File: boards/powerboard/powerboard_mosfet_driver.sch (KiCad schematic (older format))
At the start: 3 parts

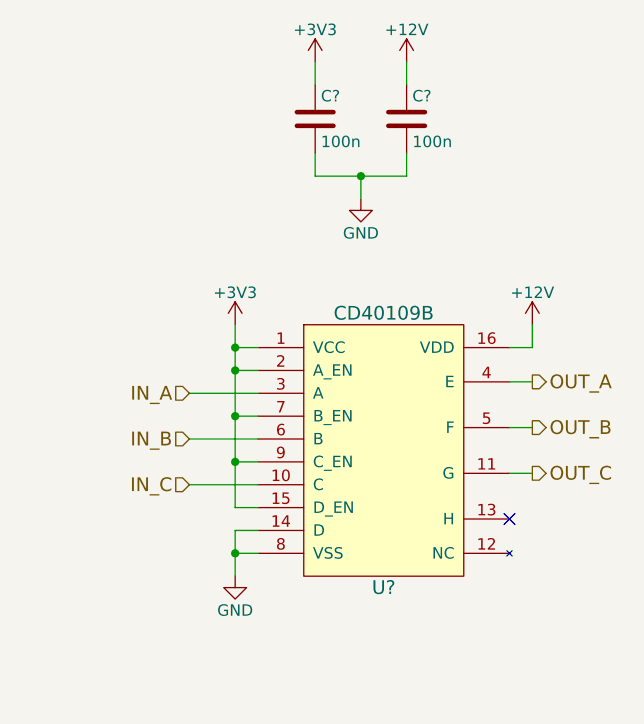
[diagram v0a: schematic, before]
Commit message: [powerboard] fix minor issues in all schematics; revision: rev10
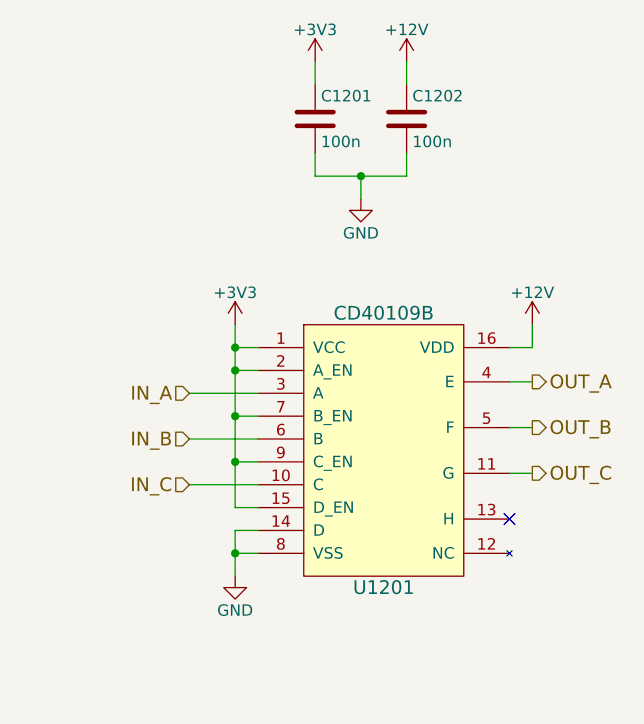
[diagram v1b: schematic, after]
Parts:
- C1201, C1202: renamed from C?; footprint (none) -> Capacitors_SMD:C_0603
- U1201: renamed from U?; footprint (none) -> Housings_SSOP:TSSOP-16_4.4x5mm_Pitch0.65mm
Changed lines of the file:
@@
 encoding utf-8
 Sheet 11 11
-Title ""
-Date ""
-Rev ""
-Comp ""
+Title "Powerboard MOSFET Driver"
+Date "2017-11-23"
+Rev "rev10"
+Comp "VIPER"
 Comment1 ""
 Comment2 ""
@@
 $EndDescr
 $Comp
-L CD40109B U?
+L CD40109B U1201
 U 1 1 5A170032
 P 5650 3950
-F 0 "U?" H 5650 3350 60  0000 C CNN
+F 0 "U1201" H 5650 3350 60  0000 C CNN
 F 1 "CD40109B" H 5650 4550 60  0000 C CNN
-F 2 "" H 5650 3900 60  0001 C CNN
+F 2 "Housings_SSOP:TSSOP-16_4.4x5mm_Pitch0.65mm" H 5650 3900 60  0001 C CNN
 F 3 "" H 5650 3900 60  0001 C CNN
 	1    5650 3950
@@
 IN_C
 $Comp
-L GND #PWR?
+L GND #PWR0115
 U 1 1 5A1700A8
 P 5000 4500
-F 0 "#PWR?" H 5000 4250 50  0001 C CNN
+F 0 "#PWR0115" H 5000 4250 50  0001 C CNN
 F 1 "GND" H 5000 4350 50  0000 C CNN
 F 2 "" H 5000 4500 50  0001 C CNN
@@
 	5000 4400 5100 4400
 $Comp
-L +3V3 #PWR?
+L +3V3 #PWR0116
 U 1 1 5A170162
 P 5000 3400
-F 0 "#PWR?" H 5000 3250 50  0001 C CNN
+F 0 "#PWR0116" H 5000 3250 50  0001 C CNN
 F 1 "+3V3" H 5000 3540 50  0000 C CNN
 F 2 "" H 5000 3400 50  0001 C CNN
@@
 $EndComp
 $Comp
-L +12V #PWR?
+L +12V #PWR0117
 U 1 1 5A170178
 P 6300 3400
-F 0 "#PWR?" H 6300 3250 50  0001 C CNN
+F 0 "#PWR0117" H 6300 3250 50  0001 C CNN
 F 1 "+12V" H 6300 3540 50  0000 C CNN
 F 2 "" H 6300 3400 50  0001 C CNN
@@
 	4800 4100 5100 4100
 $Comp
-L C C?
+L C C1201
 U 1 1 5A180FA1
 P 5350 2500
-F 0 "C?" H 5375 2600 50  0000 L CNN
+F 0 "C1201" H 5375 2600 50  0000 L CNN
 F 1 "100n" H 5375 2400 50  0000 L CNN
-F 2 "" H 5388 2350 50  0001 C CNN
+F 2 "Capacitors_SMD:C_0603" H 5388 2350 50  0001 C CNN
 F 3 "" H 5350 2500 50  0001 C CNN
 	1    5350 2500
@@
 $EndComp
 $Comp
-L C C?
+L C C1202
 U 1 1 5A181036
 P 5750 2500
-F 0 "C?" H 5775 2600 50  0000 L CNN
+F 0 "C1202" H 5775 2600 50  0000 L CNN
 F 1 "100n" H 5775 2400 50  0000 L CNN
-F 2 "" H 5788 2350 50  0001 C CNN
+F 2 "Capacitors_SMD:C_0603" H 5788 2350 50  0001 C CNN
 F 3 "" H 5750 2500 50  0001 C CNN
 	1    5750 2500
@@
 $EndComp
 $Comp
-L GND #PWR?
+L GND #PWR0118
 U 1 1 5A181058
 P 5550 2850
-F 0 "#PWR?" H 5550 2600 50  0001 C CNN
+F 0 "#PWR0118" H 5550 2600 50  0001 C CNN
 F 1 "GND" H 5550 2700 50  0000 C CNN
 F 2 "" H 5550 2850 50  0001 C CNN
@@
 Connection ~ 5550 2750
 $Comp
-L +3V3 #PWR?
+L +3V3 #PWR0119
 U 1 1 5A1810CD
 P 5350 2250
-F 0 "#PWR?" H 5350 2100 50  0001 C CNN
+F 0 "#PWR0119" H 5350 2100 50  0001 C CNN
 F 1 "+3V3" H 5350 2390 50  0000 C CNN
 F 2 "" H 5350 2250 50  0001 C CNN
@@
 $EndComp
 $Comp
-L +12V #PWR?
+L +12V #PWR0120
 U 1 1 5A1810E1
 P 5750 2250
-F 0 "#PWR?" H 5750 2100 50  0001 C CNN
+F 0 "#PWR0120" H 5750 2100 50  0001 C CNN
 F 1 "+12V" H 5750 2390 50  0000 C CNN
 F 2 "" H 5750 2250 50  0001 C CNN

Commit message: [powerboard] layout rev10; some changes to the schematic
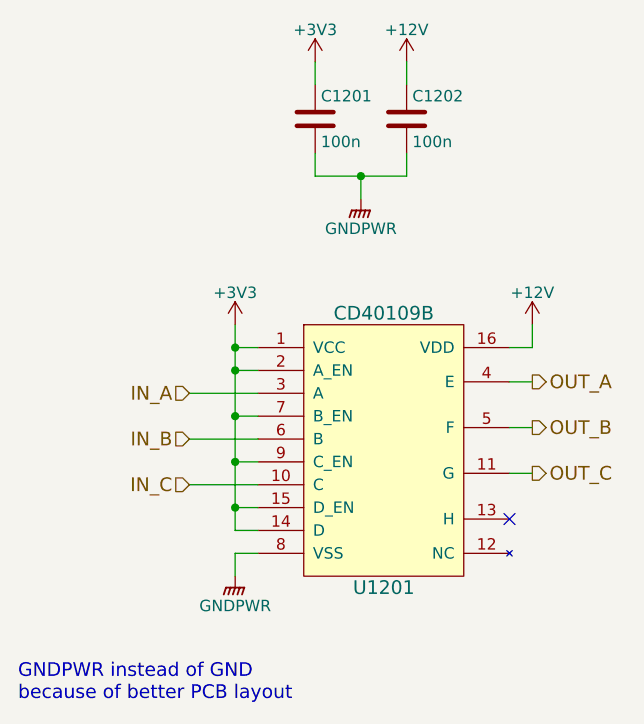
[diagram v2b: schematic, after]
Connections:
- net +3V3: now also U1201.14 (D)
- net GND renamed GNDPWR
- net GNDPWR: no longer U1201.14 (D)
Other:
- note added: "GNDPWR instead of GND\nbecause of better PCB layout"
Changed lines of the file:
@@
 IN_C
 $Comp
-L GND #PWR0115
-U 1 1 5A1700A8
-P 5000 4500
-F 0 "#PWR0115" H 5000 4250 50  0001 C CNN
-F 1 "GND" H 5000 4350 50  0000 C CNN
-F 2 "" H 5000 4500 50  0001 C CNN
-F 3 "" H 5000 4500 50  0001 C CNN
-	1    5000 4500
-	1    0    0    -1
-$EndComp
-Wire Wire Line
-	5000 4300 5000 4500
-Wire Wire Line
-	5000 4400 5100 4400
-$Comp
-L +3V3 #PWR0116
+L +3V3 #PWR0119
 U 1 1 5A170162
 P 5000 3400
-F 0 "#PWR0116" H 5000 3250 50  0001 C CNN
+F 0 "#PWR0119" H 5000 3250 50  0001 C CNN
 F 1 "+3V3" H 5000 3540 50  0000 C CNN
 F 2 "" H 5000 3400 50  0001 C CNN
@@
 $EndComp
 $Comp
-L +12V #PWR0117
+L +12V #PWR0120
 U 1 1 5A170178
 P 6300 3400
-F 0 "#PWR0117" H 6300 3250 50  0001 C CNN
+F 0 "#PWR0120" H 6300 3250 50  0001 C CNN
 F 1 "+12V" H 6300 3540 50  0000 C CNN
 F 2 "" H 6300 3400 50  0001 C CNN
@@
 	1    0    0    -1
 $EndComp
-Wire Wire Line
-	6300 3400 6300 3500
-Wire Wire Line
-	6300 3500 6200 3500
-Wire Wire Line
-	5100 3500 5000 3500
-Wire Wire Line
-	5000 3400 5000 4200
 Text HLabel 6300 3650 2    60   Output ~ 0
 OUT_A
@@
 Text HLabel 6300 4050 2    60   Output ~ 0
 OUT_C
-Wire Wire Line
-	6200 3650 6300 3650
-Wire Wire Line
-	6300 3850 6200 3850
-Wire Wire Line
-	6200 4050 6300 4050
-Wire Wire Line
-	5000 3600 5100 3600
-Connection ~ 5000 3500
-Wire Wire Line
-	5000 3800 5100 3800
-Connection ~ 5000 3600
-Wire Wire Line
-	5000 4000 5100 4000
-Connection ~ 5000 3800
-Wire Wire Line
-	5000 4200 5100 4200
-Connection ~ 5000 4000
-Wire Wire Line
-	4800 3700 5100 3700
-Wire Wire Line
-	5100 3900 4800 3900
-Wire Wire Line
-	4800 4100 5100 4100
 $Comp
 L C C1201
@@
 $EndComp
 $Comp
-L GND #PWR0118
-U 1 1 5A181058
-P 5550 2850
-F 0 "#PWR0118" H 5550 2600 50  0001 C CNN
-F 1 "GND" H 5550 2700 50  0000 C CNN
-F 2 "" H 5550 2850 50  0001 C CNN
-F 3 "" H 5550 2850 50  0001 C CNN
-	1    5550 2850
+L +3V3 #PWR0121
+U 1 1 5A1810CD
+P 5350 2250
+F 0 "#PWR0121" H 5350 2100 50  0001 C CNN
+F 1 "+3V3" H 5350 2390 50  0000 C CNN
+F 2 "" H 5350 2250 50  0001 C CNN
+F 3 "" H 5350 2250 50  0001 C CNN
+	1    5350 2250
 	1    0    0    -1
 $EndComp
+$Comp
+L +12V #PWR0122
+U 1 1 5A1810E1
+P 5750 2250
+F 0 "#PWR0122" H 5750 2100 50  0001 C CNN
+F 1 "+12V" H 5750 2390 50  0000 C CNN
+F 2 "" H 5750 2250 50  0001 C CNN
+F 3 "" H 5750 2250 50  0001 C CNN
+	1    5750 2250
+	1    0    0    -1
+$EndComp
+NoConn ~ 6200 4250
+Wire Wire Line
+	5000 4400 5100 4400
+Wire Wire Line
+	6300 3400 6300 3500
+Wire Wire Line
+	6300 3500 6200 3500
+Wire Wire Line
+	5100 3500 5000 3500
+Wire Wire Line
+	6200 3650 6300 3650
+Wire Wire Line
+	6200 4050 6300 4050
+Wire Wire Line
+	5000 3600 5100 3600
+Connection ~ 5000 3500
+Wire Wire Line
+	5000 3800 5100 3800
+Connection ~ 5000 3600
+Wire Wire Line
+	5000 4000 5100 4000
+Connection ~ 5000 3800
+Wire Wire Line
+	5000 4200 5100 4200
+Connection ~ 5000 4000
+Wire Wire Line
+	5100 3900 4800 3900
+Wire Wire Line
+	4800 4100 5100 4100
 Wire Wire Line
 	5750 2750 5750 2650
@@
 	5350 2750 5350 2650
 Connection ~ 5550 2750
-$Comp
-L +3V3 #PWR0119
-U 1 1 5A1810CD
-P 5350 2250
-F 0 "#PWR0119" H 5350 2100 50  0001 C CNN
-F 1 "+3V3" H 5350 2390 50  0000 C CNN
-F 2 "" H 5350 2250 50  0001 C CNN
-F 3 "" H 5350 2250 50  0001 C CNN
-	1    5350 2250
-	1    0    0    -1
-$EndComp
-$Comp
-L +12V #PWR0120
-U 1 1 5A1810E1
-P 5750 2250
-F 0 "#PWR0120" H 5750 2100 50  0001 C CNN
-F 1 "+12V" H 5750 2390 50  0000 C CNN
-F 2 "" H 5750 2250 50  0001 C CNN
-F 3 "" H 5750 2250 50  0001 C CNN
-	1    5750 2250
-	1    0    0    -1
-$EndComp
 Wire Wire Line
 	5750 2250 5750 2350
@@
 	5350 2250 5350 2350
 Wire Wire Line
-	5100 4300 5000 4300
-Connection ~ 5000 4400
-NoConn ~ 6200 4250
+	5000 4400 5000 4500
+Wire Wire Line
+	4800 3700 5100 3700
+Wire Wire Line
+	6300 3850 6200 3850
+Connection ~ 5000 4200
+Wire Wire Line
+	5000 3400 5000 4300
+Wire Wire Line
+	5000 4300 5100 4300
+$Comp
+L GNDPWR #PWR0123
+U 1 1 5A1C1A43
+P 5550 2850
+F 0 "#PWR0123" H 5550 2650 50  0001 C CNN
+F 1 "GNDPWR" H 5550 2720 50  0000 C CNN
+F 2 "" H 5550 2800 50  0001 C CNN
+F 3 "" H 5550 2800 50  0001 C CNN
+	1    5550 2850
+	1    0    0    -1
+$EndComp
+$Comp
+L GNDPWR #PWR0124
+U 1 1 5A1C1A67
+P 5000 4500
+F 0 "#PWR0124" H 5000 4300 50  0001 C CNN
+F 1 "GNDPWR" H 5000 4370 50  0000 C CNN
+F 2 "" H 5000 4450 50  0001 C CNN
+F 3 "" H 5000 4450 50  0001 C CNN
+	1    5000 4500
+	1    0    0    -1
+$EndComp
+Text Notes 4050 5050 0    60   ~ 0
+GNDPWR instead of GND\nbecause of better PCB layout
 $EndSCHEMATC

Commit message: [board][powerboard] Update Board to rev11
* Increase distance between 12V-Regulator and Mounting Hole
* Add TVS diode SMAJ36A to 12V regulator input
* Populate C120 (50SVPK68M)
* Add RC-filter to Hall-Sensor lines
  * f_g = 7kHz (470 ohms, 22nF)
* End Switch Pull-Down
* Hall-Sensor Pull-Up
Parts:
- C1201, C1202: symbol C -> powerboard-rescue:C
- U1201: symbol CD40109B -> cd40109b:CD40109B
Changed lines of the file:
@@
-EESchema Schematic File Version 2
-LIBS:powerboard-rescue
-LIBS:power
-LIBS:device
-LIBS:transistors
-LIBS:conn
-LIBS:linear
-LIBS:regul
-LIBS:74xx
-LIBS:cmos4000
-LIBS:adc-dac
-LIBS:memory
-LIBS:xilinx
-LIBS:microcontrollers
-LIBS:dsp
-LIBS:microchip
-LIBS:analog_switches
-LIBS:motorola
-LIBS:texas
-LIBS:intel
-LIBS:audio
-LIBS:interface
-LIBS:digital-audio
-LIBS:philips
-LIBS:display
-LIBS:cypress
-LIBS:siliconi
-LIBS:opto
-LIBS:atmel
-LIBS:contrib
-LIBS:valves
-LIBS:TI-LMZ1xxxx
-LIBS:DRV8816
-LIBS:ACS711
-LIBS:lt1370
-LIBS:lt3757
-LIBS:common_mode_choke
-LIBS:ltc4010
-LIBS:pc3h7
-LIBS:esd_diode_dual
-LIBS:ad7928
-LIBS:references
-LIBS:lt3592
-LIBS:ds26lv32at
-LIBS:drv8312
-LIBS:drv8332
-LIBS:cd40109b
+EESchema Schematic File Version 4
 LIBS:powerboard-cache
-EELAYER 25 0
+EELAYER 26 0
 EELAYER END
 $Descr A4 11693 8268
@@
 Title "Powerboard MOSFET Driver"
 Date "2017-11-23"
-Rev "rev10"
+Rev "rev11"
 Comp "VIPER"
 Comment1 ""
@@
 $EndDescr
 $Comp
-L CD40109B U1201
+L cd40109b:CD40109B U1201
 U 1 1 5A170032
 P 5650 3950
@@
 IN_C
 $Comp
-L +3V3 #PWR0119
+L power1:+3V3 #PWR0119
 U 1 1 5A170162
 P 5000 3400
@@
 $EndComp
 $Comp
-L +12V #PWR0120
+L power1:+12V #PWR0120
 U 1 1 5A170178
 P 6300 3400
@@
 OUT_C
 $Comp
-L C C1201
+L powerboard-rescue:C C1201
 U 1 1 5A180FA1
 P 5350 2500
+AR Path="/5A180FA1" Ref="C1201"  Part="1"
+AR Path="/5A16D393/5A180FA1" Ref="C1201"  Part="1"
 F 0 "C1201" H 5375 2600 50  0000 L CNN
 F 1 "100n" H 5375 2400 50  0000 L CNN
@@
 $EndComp
 $Comp
-L C C1202
+L powerboard-rescue:C C1202
 U 1 1 5A181036
 P 5750 2500
+AR Path="/5A181036" Ref="C1202"  Part="1"
+AR Path="/5A16D393/5A181036" Ref="C1202"  Part="1"
 F 0 "C1202" H 5775 2600 50  0000 L CNN
 F 1 "100n" H 5775 2400 50  0000 L CNN
@@
 $EndComp
 $Comp
-L +3V3 #PWR0121
+L power1:+3V3 #PWR0121
 U 1 1 5A1810CD
 P 5350 2250
@@
 $EndComp
 $Comp
-L +12V #PWR0122
+L power1:+12V #PWR0122
 U 1 1 5A1810E1
 P 5750 2250
@@
 	5000 4300 5100 4300
 $Comp
-L GNDPWR #PWR0123
+L powerboard-rescue:GNDPWR #PWR0123
 U 1 1 5A1C1A43
 P 5550 2850
@@
 $EndComp
 $Comp
-L GNDPWR #PWR0124
+L powerboard-rescue:GNDPWR #PWR0124
 U 1 1 5A1C1A67
 P 5000 4500
